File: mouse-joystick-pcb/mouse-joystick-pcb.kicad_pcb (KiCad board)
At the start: 4 copper layers, 60 x 120 mm, 88 parts, among them J301 2.1, J501 Conn_01x02_P3.5mm_TBH_Horizon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, J502 Conn_01x04_P3.5mm_TBH_Horizon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, J503 Conn_01x05_P3.5mm_TBH_Horizon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, J701 Conn_01x02_P3.5mm_TBH_Horizon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, J702 Conn_01x04_P3.5mm_TBH_Horizon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, J801 Conn_01x02_P3.5mm_TBH_Horizon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, J901 Conn_01x04_P3.5mm_TBH_Horizon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, U301 TPSM365R6V5RDNR, U501 MAX6816, U502 TMC5130A-TA, U503 Logic_LevelTranslator_LSF0102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, U601 TPA6204A1DRBR, U701 MAX6816, U702 TMC5130A-TA, U801 40V_200mA, U901 PGA305ARHHR, X501 16MHz_3.3V, X701 16MHz_3.3V

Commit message: Complete some routing
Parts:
- moved C516 4.81 mm to (118.2, 92.8)
- moved C508 2.02 mm to (118.4, 87.3), turned to 0 degrees
- moved R504 2.02 mm to (116.4, 87.3), turned to 0 degrees
- moved C511 1.46 mm to (116.7, 92.8), turned to -90 degrees
- moved R402 0.50 mm to (103.9, 55.6)
- moved R401 0.25 mm to (102.7, 55.6)
- moved R801 0.25 mm to (113.4, 109.3)
- moved U801 0.25 mm to (116.4, 109.3)
- turned C503 to 180 degrees
- turned R703 to 180 degrees
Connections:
- J901 pad 1: /torque-sensor/BRG+ -> /torque-sensor/BRG-
- J901 pad 2: /torque-sensor/INP- -> /torque-sensor/BRG+
- J901 pad 3: /torque-sensor/INP+ -> /torque-sensor/INP-
- J901 pad 4: /torque-sensor/BRG- -> /torque-sensor/INP+
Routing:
- net /GND: track 0.00 -> 618.2 mm, vias 0 -> 3
- net /VAA: track 0.00 -> 101.7 mm
- net /MOTOR_DIAG0_1: track 0.00 -> 93.5 mm, vias 0 -> 1
- net /COPI: track 0.00 -> 93.0 mm, vias 0 -> 1
- net /CIPO: track 0.00 -> 89.2 mm, vias 0 -> 1
- net /~{MOTOR_CS_1}: track 0.00 -> 83.1 mm
- net /SCK: track 0.00 -> 67.1 mm, vias 0 -> 1
- net /+5V: track 0.00 -> 48.7 mm
- net /+3.3V: track 0.00 -> 45.8 mm, vias 0 -> 2
- net /motor-1/REFL_DEBOUNCED: track 0.00 -> 33.6 mm, vias 0 -> 2
- net /motor-0/REFL_DEBOUNCED: track 0.00 -> 32.8 mm, vias 0 -> 2
- net /MOTOR_DIAG0_0: track 0.00 -> 22.3 mm, vias 0 -> 1
- net /motor-0/BMB1: track 0.00 -> 22.1 mm, vias 0 -> 1
- net /motor-0/BMA1: track 0.00 -> 20.2 mm, vias 0 -> 1
- net /motor-1/BMB1: track 0.00 -> 19.0 mm, vias 0 -> 1
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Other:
- copper layers 4 -> 2

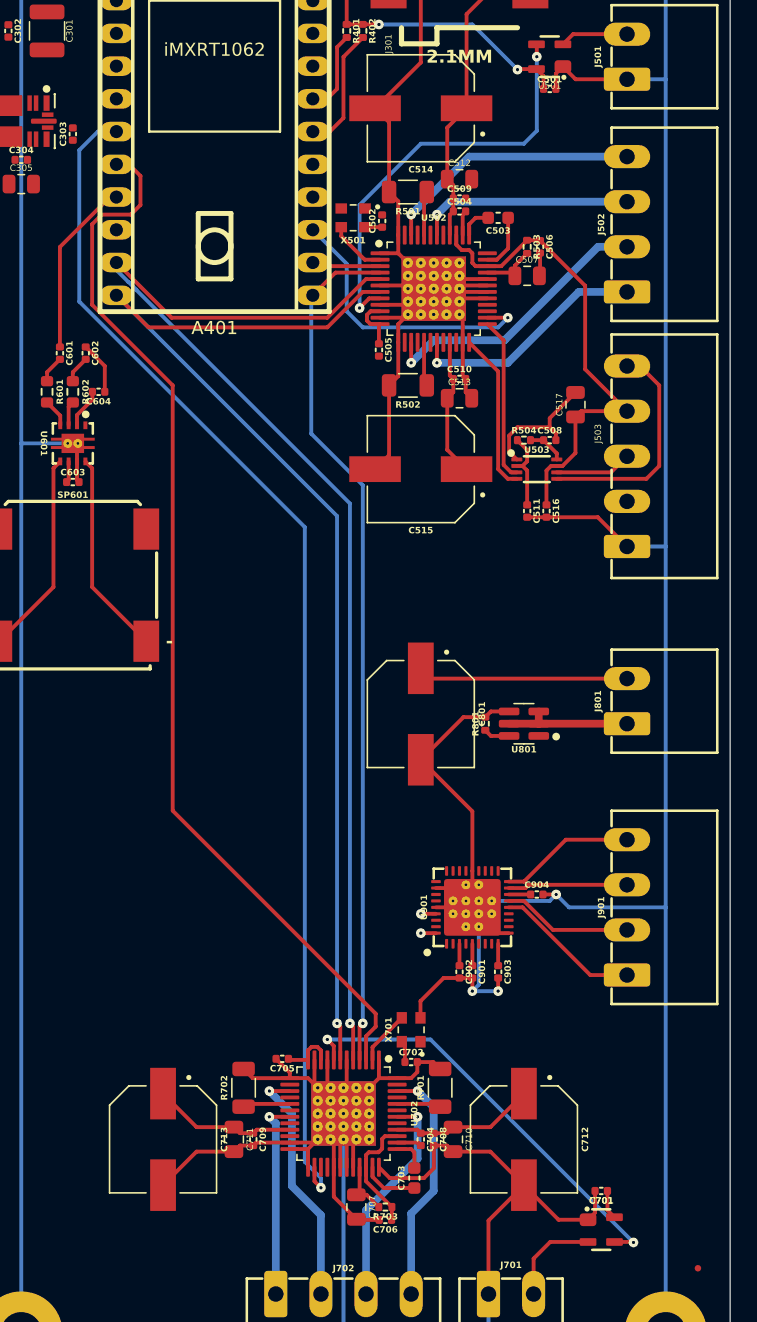
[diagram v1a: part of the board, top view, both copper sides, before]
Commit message: Change encoder connector
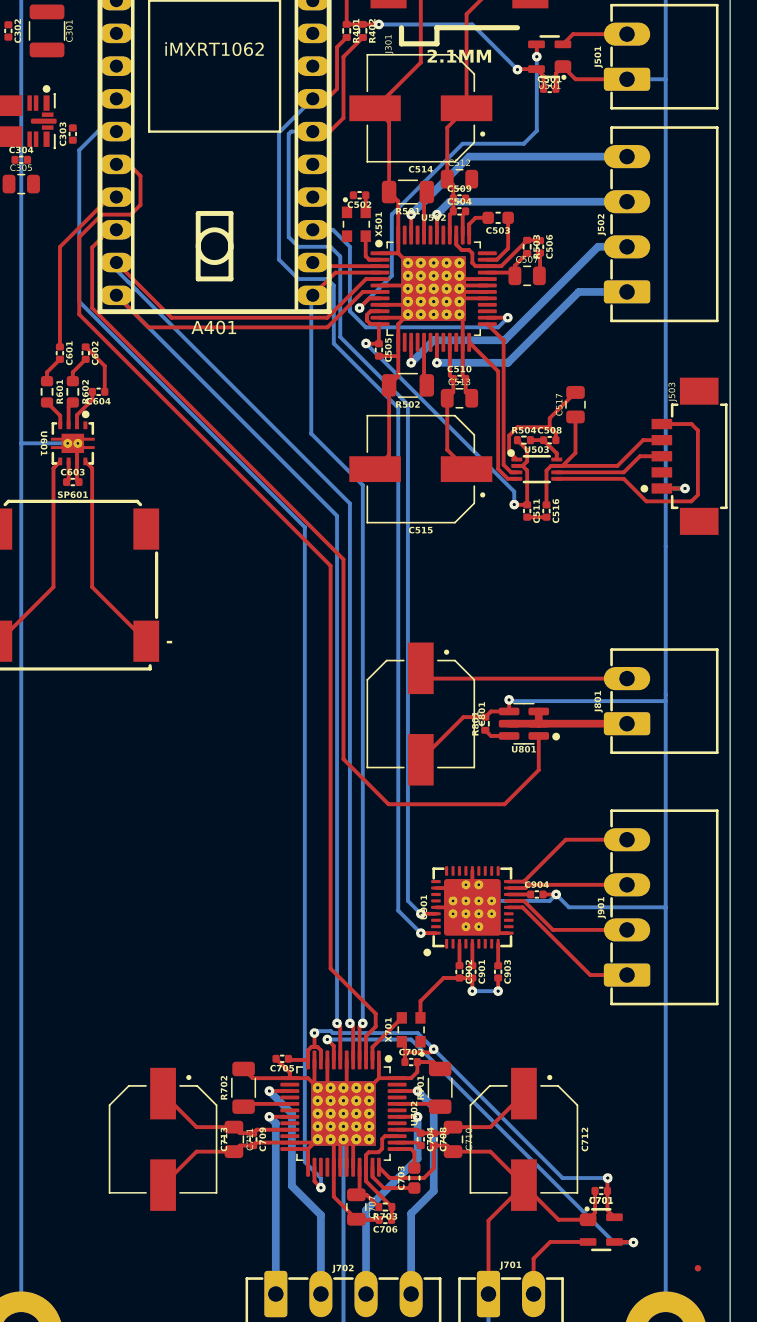
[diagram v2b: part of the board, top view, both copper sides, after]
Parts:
- J503: value Conn_01x05_P3.5mm_TBH_Horizontal_Screw -> Molex_PicoBlade_Horizontal; footprint Janelia:PhoenixContact_MC_1,5_5-G-3.5_1x05_P3.50mm_Horizontal_Screw -> Janelia:MOLEX_0532610571
- moved J503 3.50 mm to (127.9, 88.6)
- moved C502 2.66 mm to (103.7, 68.3), turned to 180 degrees
- moved X501 0.56 mm to (103.4, 70.6), turned to -90 degrees
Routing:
- net /SCL: track 7.67 -> 79.4 mm
- net /BRAKE_PWM: track 0.00 -> 70.6 mm
- net /SDA: track 10.9 -> 79.0 mm
- net /+3.3V: track 45.8 -> 97.1 mm, vias 2 -> 7
- net /+5V: track 48.7 -> 37.5 mm
- net /GND: track 618.2 -> 610.4 mm, vias 3 -> 5
- net /motor-0/ENC_A: track 5.97 -> 8.67 mm
- net /motor-0/ENC_B: track 17.7 -> 19.9 mm
- net /motor-0/REFL_DEBOUNCED: track 32.8 -> 30.8 mm
- net /motor-0/CLOCK: track 4.47 -> 2.78 mm
- net /~{MOTOR_CS_1}: track 83.1 -> 84.0 mm
- net /MOTOR_DIAG0_0: track 22.3 -> 23.1 mm

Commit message: Finish routing
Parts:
- added R505: 1.8k, Janelia:R_0402_1005Metric, F.Cu at (103.7, 67.3)
- added R704: 1.8k, Janelia:R_0402_1005Metric, F.Cu at (100.2, 131.6)
- added REF**: Polarity_Center_Positive_0.5mm_SilkScreen, Janelia:Polarity_Center_Positive_0.5mm_SilkScreen, F.Cu at (126.4, 51.1)
- moved C801 4.00 mm to (108.4, 104.6)
- moved J801 4.00 mm to (124.4, 103.6)
- moved R801 4.00 mm to (113.4, 105.3)
- moved U801 4.00 mm to (116.4, 105.3)
- moved C508 3.04 mm to (117.9, 84.3)
- moved C511 3.04 mm to (116.2, 89.8)
- moved C516 3.04 mm to (117.7, 89.8)
- moved C517 3.04 mm to (119.9, 81.6)
- moved J503 3.04 mm to (127.4, 85.6)
- moved R504 3.04 mm to (115.9, 84.3)
- moved U503 3.04 mm to (116.9, 86.6)
- moved C501 1.50 mm to (116.9, 60.1)
- moved U501 1.50 mm to (116.9, 57.6)
- moved C303 0.71 mm to (80.9, 64.1)
- moved C514 0.25 mm to (108.7, 61.6)
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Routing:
- net /VAA: track 101.7 -> 367.4 mm
- net /+5V: track 37.5 -> 227.2 mm, vias 0 -> 6
- net /GND: track 610.4 -> 789.0 mm, vias 5 -> 10
- net /+3.3V: track 97.1 -> 207.1 mm, vias 7 -> 8
- net /~{MOTOR_CS_0}: track 5.33 -> 12.3 mm
- net /power/VDD: track 0.00 -> 6.66 mm
- net /BRAKE_PWM: track 70.6 -> 64.8 mm, vias 0 -> 1
- net /motor-0/ENC_B_LS: track 12.5 -> 9.62 mm
- net /motor-0/ENC_A_LS: track 12.7 -> 9.80 mm
- net /motor-0/REFL_DEBOUNCED: track 30.8 -> 28.1 mm
- net /~{MOTOR_CS_1}: track 84.0 -> 85.9 mm, vias 0 -> 1
- net /motor-0/REFL: track 5.30 -> 6.80 mm
- net /AUDIO: track 13.7 -> 14.5 mm
- net /motor-1/BMA1: track 18.6 -> 19.2 mm
- added copper zone on B.Cu, net /GND
- added copper zone on In1.Cu, net /GND
- added copper zone on In2.Cu, net /GND
- added copper zone on F.Cu, net /VAA
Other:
- copper layers 2 -> 4
- board text added: "+24V"
- board text added: "+5V"
- board text added: "BASE"
- board text added: "BLK"
- board text added: "BLU"
- board text added: "BRAKE"
- board text added: "ENCODER"
- board text added: "ENC_A"
- board text added: "ENC_B"
- board text added: "GND"
- board text added: "GRN"
- board text added: "JOYSTICK"
- board text added: "RED"
- board text added: "REFL"
- board text added: "TORQUE SENSOR"
- board text added: "WHT"
- board text removed: "+24VDC Center Positive"

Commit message: Generate metadata
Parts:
- removed REF**: Polarity_Center_Positive_0.5mm_SilkScreen, Janelia:Polarity_Center_Positive_0.5mm_SilkScreen
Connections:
- net /MOTOR_DIAG0_0 renamed /JOYSTICK_MOTOR_DIAG0
- net /MOTOR_DIAG0_1 renamed /BASE_MOTOR_DIAG0
- net /motor-0/5VOUT renamed /joystick-motor/5VOUT
- net /motor-0/BMA1 renamed /joystick-motor/BMA1
- net /motor-0/BMA2 renamed /joystick-motor/BMA2
- net /motor-0/BMB1 renamed /joystick-motor/BMB1
- net /motor-0/BMB2 renamed /joystick-motor/BMB2
- net /motor-0/BRA renamed /joystick-motor/BRA
- net /motor-0/BRB renamed /joystick-motor/BRB
- net /motor-0/CLOCK renamed /joystick-motor/CLOCK
- net /motor-0/CPI renamed /joystick-motor/CPI
- net /motor-0/CPO renamed /joystick-motor/CPO
- net /motor-0/EN renamed /joystick-motor/EN
- net /motor-0/ENC_A renamed /joystick-motor/ENC_A
- net /motor-0/ENC_A_LS renamed /joystick-motor/ENC_A_LS
- net /motor-0/ENC_B renamed /joystick-motor/ENC_B
- net /motor-0/ENC_B_LS renamed /joystick-motor/ENC_B_LS
- net /motor-0/REFL renamed /joystick-motor/REFL
- net /motor-0/REFL_DEBOUNCED renamed /joystick-motor/REFL_DEBOUNCED
- net /motor-0/VCP renamed /joystick-motor/VCP
- net /motor-1/5VOUT renamed /base-motor/5VOUT
- net /motor-1/BMA1 renamed /base-motor/BMA1
- net /motor-1/BMA2 renamed /base-motor/BMA2
- net /motor-1/BMB1 renamed /base-motor/BMB1
- net /motor-1/BMB2 renamed /base-motor/BMB2
- net /motor-1/BRA renamed /base-motor/BRA
- net /motor-1/BRB renamed /base-motor/BRB
- net /motor-1/CLOCK renamed /base-motor/CLOCK
- net /motor-1/CPI renamed /base-motor/CPI
- net /motor-1/CPO renamed /base-motor/CPO
- net /motor-1/REFL renamed /base-motor/REFL
- net /motor-1/REFL_DEBOUNCED renamed /base-motor/REFL_DEBOUNCED
- net /motor-1/VCP renamed /base-motor/VCP
- net /~{MOTOR_CS_0} renamed /~{JOYSTICK_MOTOR_CS}
- net /~{MOTOR_CS_1} renamed /~{BASE_MOTOR_CS}

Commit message: Switch LED resistor to 1.5k
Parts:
- R301: value 2.32k -> 1.5k
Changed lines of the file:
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@@
     (descr "Resistor SMD 0805 (2012 Metric), square (rectangular) end terminal, IPC_7351 nominal, (Body size source: IPC-SM-782 page 72, https://www.pcb-3d.com/wordpress/wp-content/uploads/ipc-sm-782a_amendment_1_and_2.pdf), generated with kicad-footprint-generator")
     (tags "resistor")
-    (property "LCSC" "C3961061")
-    (property "Manufacturer" "TE Connectivity Passive Product")
-    (property "Manufacturer Part Number" "RA73F2A2K32BTD")
+    (property "LCSC" "C417005")
+    (property "Manufacturer" "PANASONIC")
+    (property "Manufacturer Part Number" "ERJP06J152V")
     (property "Package" "0805")
     (property "Sheetfile" "power.kicad_sch")
     (property "Sheetname" "power")
-    (property "Synopsis" "RA73F 2A 2K32 0.1% 5K RL")
+    (property "Synopsis" "RES SMD 1.5K OHM 5% 500mW")
     (property "Vendor" "Digi-Key")
-    (property "Vendor Part Number" "1712-RA73F2A2K32BTDCT-ND")
-    (property "ki_description" "2.32 kOhms ±0.1% 1W Chip Resistor 0805 (2012 Metric) Thin Film")
+    (property "Vendor Part Number" "P1.5KADCT-ND")
+    (property "ki_description" "500mW Thick Film Resistors 600V ±5% ±200ppm/℃ 1.5kΩ 0805 Chip Resistor - Surface Mount ROHS")
     (attr smd)
     (fp_text reference "R301" (at -2 0 -180) (layer "F.SilkS")
         (effects (font (size 0.5 0.5) (thickness 0.125) bold))
     )
-    (fp_text value "2.32k" (at 0 1.25 90) (layer "F.Fab")
+    (fp_text value "1.5k" (at 0 1.25 90) (layer "F.Fab")
         (effects (font (size 0.5 0.5) (thickness 0.125) bold))
     )

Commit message: Update all fabrication files
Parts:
- moved H201 0.13 mm to (77.4, 46.6)
- moved H202 0.13 mm to (127.4, 46.6)
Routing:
- net /COPI: track 93.0 -> 94.8 mm
- net /~{BASE_MOTOR_CS}: track 85.9 -> 84.3 mm
- net /CIPO: track 89.2 -> 90.2 mm
- net /SCL: track 79.4 -> 80.3 mm
- net /BRAKE_PWM: track 64.8 -> 65.7 mm
- net /BASE_MOTOR_DIAG0: track 93.5 -> 94.3 mm
